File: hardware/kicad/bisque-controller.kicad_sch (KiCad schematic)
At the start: 52 parts, among them J1 USB-C, J2 5V_IN, J3 TC_K, J4 SSR, J5 DISPLAY, J6 NAV_SW, J7 AUX, Q1 AO3400A, Q2 AO3400A, SW1 RESET, SW2 BOOT, U1 ESP32-S3-WROOM-1-N16R8, U2 AMS1117-3.3, U3 MAX31855KASA+, U4 USBLC6-2SC6

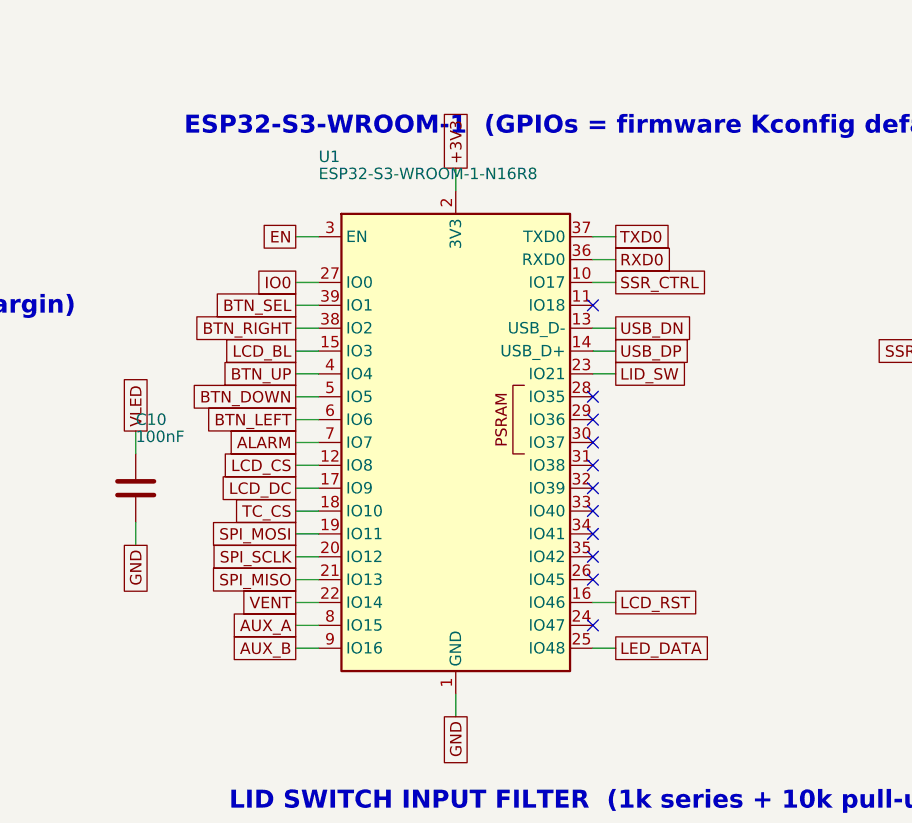
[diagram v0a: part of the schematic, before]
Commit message: feat(hw)!: re-map GPIOs for rev B
Buttons to 38-42 (contiguous module pads), lid to GPIO 4, SSR2 onto 21,
TC2/watchdog onto the pins quad PSRAM freed. check_pinmap.py now passes.
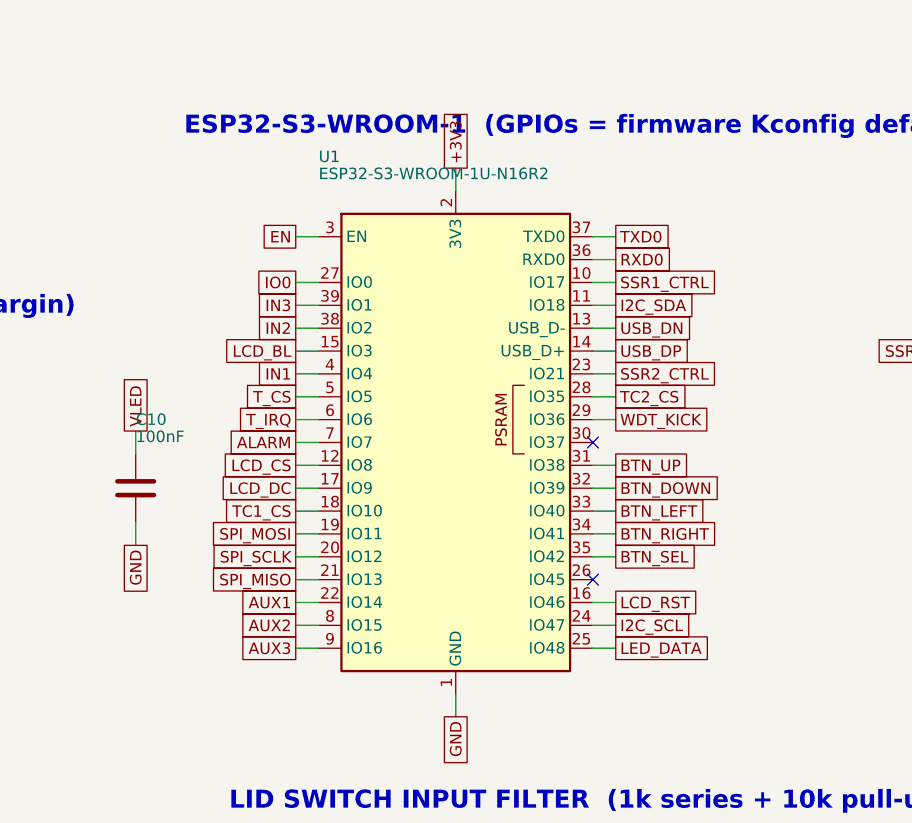
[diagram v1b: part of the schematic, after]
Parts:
- U1: value ESP32-S3-WROOM-1-N16R8 -> ESP32-S3-WROOM-1U-N16R2; footprint RF_Module:ESP32-S3-WROOM-1 -> RF_Module:ESP32-S3-WROOM-1U
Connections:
- net AUX_A: no longer U1.8 (IO15)
- net AUX_B: no longer U1.9 (IO16)
- net BTN_DOWN: now also U1.32 (IO39); no longer U1.5 (IO5)
- net BTN_LEFT: now also U1.33 (IO40); no longer U1.6 (IO6)
- net BTN_RIGHT: now also U1.34 (IO41); no longer U1.38 (IO2)
- net BTN_SEL: now also U1.35 (IO42); no longer U1.39 (IO1)
- net BTN_UP: now also U1.31 (IO38); no longer U1.4 (IO4)
- net LID_SW: no longer U1.23 (IO21)
- net SSR_CTRL: no longer U1.10 (IO17)
- net TC_CS: no longer U1.18 (IO10)
- net VENT: no longer U1.22 (IO14)
- net I2C_SDA: now reaches U1.11 (IO18)
- net I2C_SCL: now reaches U1.24 (IO47)
- net TC2_CS: now reaches U1.28 (IO35)
- net WDT_KICK: now reaches U1.29 (IO36)
- new net AUX1: U1.22 (IO14)
- new net AUX2: U1.8 (IO15)
- new net AUX3: U1.9 (IO16)
- new net IN1: U1.4 (IO4)
- new net IN2: U1.38 (IO2)
- new net IN3: U1.39 (IO1)
- new net SSR1_CTRL: U1.10 (IO17)
- new net SSR2_CTRL: U1.23 (IO21)
- new net TC1_CS: U1.18 (IO10)
- new net T_CS: U1.5 (IO5)
- new net T_IRQ: U1.6 (IO6)
- no-connect marks 15 -> 6
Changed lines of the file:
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@@
 			(effects (font (size 1.27 1.27)) (justify left))
 		)
-		(property "Value" "ESP32-S3-WROOM-1-N16R8" (at 154.94 135.25 0)
+		(property "Value" "ESP32-S3-WROOM-1U-N16R2" (at 154.94 135.25 0)
 			(effects (font (size 1.27 1.27)) (justify left))
 		)
-		(property "Footprint" "RF_Module:ESP32-S3-WROOM-1" (at 170.18 165.1 0)
+		(property "Footprint" "RF_Module:ESP32-S3-WROOM-1U" (at 170.18 165.1 0)
 			(effects (font (size 1.27 1.27)) hide)
 		)
@@
 		(stroke (width 0) (type default))
 	)
-	(global_label "BTN_UP" (shape passive) (at 152.4 157.48 180)
+	(global_label "IN1" (shape passive) (at 152.4 157.48 180)
 		(effects (font (size 1.27 1.27)) (justify right))
 		(property "Intersheetrefs" "${INTERSHEET_REFS}" (at 152.4 157.48 0)
@@
 		(stroke (width 0) (type default))
 	)
-	(global_label "BTN_DOWN" (shape passive) (at 152.4 160.02 180)
+	(global_label "T_CS" (shape passive) (at 152.4 160.02 180)
 		(effects (font (size 1.27 1.27)) (justify right))
 		(property "Intersheetrefs" "${INTERSHEET_REFS}" (at 152.4 160.02 0)
@@
 		(stroke (width 0) (type default))
 	)
-	(global_label "BTN_LEFT" (shape passive) (at 152.4 162.56 180)
+	(global_label "T_IRQ" (shape passive) (at 152.4 162.56 180)
 		(effects (font (size 1.27 1.27)) (justify right))
 		(property "Intersheetrefs" "${INTERSHEET_REFS}" (at 152.4 162.56 0)
@@
 		(stroke (width 0) (type default))
 	)
-	(global_label "AUX_A" (shape passive) (at 152.4 185.42 180)
+	(global_label "AUX2" (shape passive) (at 152.4 185.42 180)
 		(effects (font (size 1.27 1.27)) (justify right))
 		(property "Intersheetrefs" "${INTERSHEET_REFS}" (at 152.4 185.42 0)
@@
 		(stroke (width 0) (type default))
 	)
-	(global_label "AUX_B" (shape passive) (at 152.4 187.96 180)
+	(global_label "AUX3" (shape passive) (at 152.4 187.96 180)
 		(effects (font (size 1.27 1.27)) (justify right))
 		(property "Intersheetrefs" "${INTERSHEET_REFS}" (at 152.4 187.96 0)
@@
 		(stroke (width 0) (type default))
 	)
-	(global_label "SSR_CTRL" (shape passive) (at 187.96 147.32 0)
+	(global_label "SSR1_CTRL" (shape passive) (at 187.96 147.32 0)
 		(effects (font (size 1.27 1.27)) (justify left))
 		(property "Intersheetrefs" "${INTERSHEET_REFS}" (at 187.96 147.32 0)
@@
 		)
 	)
-	(no_connect (at 185.42 149.86))
+	(wire (pts (xy 185.42 149.86) (xy 187.96 149.86))
+		(stroke (width 0) (type default))
+	)
+	(global_label "I2C_SDA" (shape passive) (at 187.96 149.86 0)
+		(effects (font (size 1.27 1.27)) (justify left))
+		(property "Intersheetrefs" "${INTERSHEET_REFS}" (at 187.96 149.86 0)
+			(effects (font (size 1.27 1.27)) hide)
+		)
+	)
 	(wire (pts (xy 154.94 167.64) (xy 152.4 167.64))
 		(stroke (width 0) (type default))
@@
 		(stroke (width 0) (type default))
 	)
-	(global_label "TC_CS" (shape passive) (at 152.4 172.72 180)
+	(global_label "TC1_CS" (shape passive) (at 152.4 172.72 180)
 		(effects (font (size 1.27 1.27)) (justify right))
 		(property "Intersheetrefs" "${INTERSHEET_REFS}" (at 152.4 172.72 0)
@@
 		(stroke (width 0) (type default))
 	)
-	(global_label "VENT" (shape passive) (at 152.4 182.88 180)
+	(global_label "AUX1" (shape passive) (at 152.4 182.88 180)
 		(effects (font (size 1.27 1.27)) (justify right))
 		(property "Intersheetrefs" "${INTERSHEET_REFS}" (at 152.4 182.88 0)
@@
 		(stroke (width 0) (type default))
 	)
-	(global_label "LID_SW" (shape passive) (at 187.96 157.48 0)
+	(global_label "SSR2_CTRL" (shape passive) (at 187.96 157.48 0)
 		(effects (font (size 1.27 1.27)) (justify left))
 		(property "Intersheetrefs" "${INTERSHEET_REFS}" (at 187.96 157.48 0)
@@
 		)
 	)
-	(no_connect (at 185.42 185.42))
+	(wire (pts (xy 185.42 185.42) (xy 187.96 185.42))
+		(stroke (width 0) (type default))
+	)
+	(global_label "I2C_SCL" (shape passive) (at 187.96 185.42 0)
+		(effects (font (size 1.27 1.27)) (justify left))
+		(property "Intersheetrefs" "${INTERSHEET_REFS}" (at 187.96 185.42 0)
+			(effects (font (size 1.27 1.27)) hide)
+		)
+	)
 	(wire (pts (xy 185.42 187.96) (xy 187.96 187.96))
 		(stroke (width 0) (type default))
@@
 		)
 	)
-	(no_connect (at 185.42 160.02))
-	(no_connect (at 185.42 162.56))
+	(wire (pts (xy 185.42 160.02) (xy 187.96 160.02))
+		(stroke (width 0) (type default))
+	)
+	(global_label "TC2_CS" (shape passive) (at 187.96 160.02 0)
+		(effects (font (size 1.27 1.27)) (justify left))
+		(property "Intersheetrefs" "${INTERSHEET_REFS}" (at 187.96 160.02 0)
+			(effects (font (size 1.27 1.27)) hide)
+		)
+	)
+	(wire (pts (xy 185.42 162.56) (xy 187.96 162.56))
+		(stroke (width 0) (type default))
+	)
+	(global_label "WDT_KICK" (shape passive) (at 187.96 162.56 0)
+		(effects (font (size 1.27 1.27)) (justify left))
+		(property "Intersheetrefs" "${INTERSHEET_REFS}" (at 187.96 162.56 0)
+			(effects (font (size 1.27 1.27)) hide)
+		)
+	)
 	(no_connect (at 185.42 165.1))
-	(no_connect (at 185.42 167.64))
-	(no_connect (at 185.42 170.18))
-	(no_connect (at 185.42 172.72))
-	(no_connect (at 185.42 175.26))
-	(no_connect (at 185.42 177.8))
+	(wire (pts (xy 185.42 167.64) (xy 187.96 167.64))
+		(stroke (width 0) (type default))
+	)
+	(global_label "BTN_UP" (shape passive) (at 187.96 167.64 0)
+		(effects (font (size 1.27 1.27)) (justify left))
+		(property "Intersheetrefs" "${INTERSHEET_REFS}" (at 187.96 167.64 0)
+			(effects (font (size 1.27 1.27)) hide)
+		)
+	)
+	(wire (pts (xy 185.42 170.18) (xy 187.96 170.18))
+		(stroke (width 0) (type default))
+	)
+	(global_label "BTN_DOWN" (shape passive) (at 187.96 170.18 0)
+		(effects (font (size 1.27 1.27)) (justify left))
+		(property "Intersheetrefs" "${INTERSHEET_REFS}" (at 187.96 170.18 0)
+			(effects (font (size 1.27 1.27)) hide)
+		)
+	)
+	(wire (pts (xy 185.42 172.72) (xy 187.96 172.72))
+		(stroke (width 0) (type default))
+	)
+	(global_label "BTN_LEFT" (shape passive) (at 187.96 172.72 0)
+		(effects (font (size 1.27 1.27)) (justify left))
+		(property "Intersheetrefs" "${INTERSHEET_REFS}" (at 187.96 172.72 0)
+			(effects (font (size 1.27 1.27)) hide)
+		)
+	)
+	(wire (pts (xy 185.42 175.26) (xy 187.96 175.26))
+		(stroke (width 0) (type default))
+	)
+	(global_label "BTN_RIGHT" (shape passive) (at 187.96 175.26 0)
+		(effects (font (size 1.27 1.27)) (justify left))
+		(property "Intersheetrefs" "${INTERSHEET_REFS}" (at 187.96 175.26 0)
+			(effects (font (size 1.27 1.27)) hide)
+		)
+	)
+	(wire (pts (xy 185.42 177.8) (xy 187.96 177.8))
+		(stroke (width 0) (type default))
+	)
+	(global_label "BTN_SEL" (shape passive) (at 187.96 177.8 0)
+		(effects (font (size 1.27 1.27)) (justify left))
+		(property "Intersheetrefs" "${INTERSHEET_REFS}" (at 187.96 177.8 0)
+			(effects (font (size 1.27 1.27)) hide)
+		)
+	)
 	(wire (pts (xy 185.42 144.78) (xy 187.96 144.78))
 		(stroke (width 0) (type default))
@@
 		(stroke (width 0) (type default))
 	)
-	(global_label "BTN_RIGHT" (shape passive) (at 152.4 152.4 180)
+	(global_label "IN2" (shape passive) (at 152.4 152.4 180)
 		(effects (font (size 1.27 1.27)) (justify right))
 		(property "Intersheetrefs" "${INTERSHEET_REFS}" (at 152.4 152.4 0)
@@
 		(stroke (width 0) (type default))
 	)
-	(global_label "BTN_SEL" (shape passive) (at 152.4 149.86 180)
+	(global_label "IN3" (shape passive) (at 152.4 149.86 180)
 		(effects (font (size 1.27 1.27)) (justify right))
 		(property "Intersheetrefs" "${INTERSHEET_REFS}" (at 152.4 149.86 0)

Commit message: feat(hw): two MAX31856 thermocouple front-ends
Replaces the MAX31855 (U3/C8/C9) with two MAX31856 channels (U3 control,
U5 load), each with separate AVDD/DVDD decoupling, a 100R 1% series R in
each T+/T- leg, and the datasheet's differential (100nF) + common-mode
(10nF x2) input filter on the IC side of those resistors. DRDY and FAULT
left NC and polled from registers to save four GPIOs.

Per REV-B-NOTES.md (datasheet-verification override of the plan): there is
no BIAS bypass capacitor - BIAS ties directly to the filtered T- node
instead, matching the MAX31856's actual application circuit. TC1_N/TC2_N
run to their screw terminals raw, not to GND, so each channel keeps its own
floating differential pair; ungrounded-junction probes are now required
(documentation obligation, tracked for a later task).

Also fixes two now-dead net-name references in gen_pcb.py's ROUTE_ORDER
(TC_P, TC_CS) left over from the old MAX31855 wiring, and adds the TSSOP-14
footprint snapshot gen_pcb.py's KiCad-free fallback path requires.
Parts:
- removed C8: 100nF, Capacitor_SMD:C_0805_2012Metric, symbol Device:C
- removed C9: 10nF, Capacitor_SMD:C_0805_2012Metric, symbol Device:C
- added C13, C14, C15, C18, C19, C20: 100nF, Capacitor_SMD:C_0805_2012Metric, symbol Device:C
- added C16, C17, C21, C22: 10nF, Capacitor_SMD:C_0805_2012Metric, symbol Device:C
- added J8: TC2_K, TerminalBlock_Phoenix:TerminalBlock_Phoenix_MKDS-1,5-2-5.08_1x02_P5.08mm_Horizontal, symbol Connector:Screw_Terminal_01x02
- added R14, R15, R16, R17: 100R 1%, Resistor_SMD:R_0805_2012Metric, symbol Device:R
- added U5: MAX31856MUD+, Package_SO:TSSOP-14_4.4x5mm_P0.65mm, symbol Sensor_Temperature:MAX31856
- J3: value TC_K -> TC1_K
- U3: value MAX31855KASA+ -> MAX31856MUD+; footprint Package_SO:SOIC-8_3.9x4.9mm_P1.27mm -> Package_SO:TSSOP-14_4.4x5mm_P0.65mm; symbol Sensor_Temperature:MAX31855KASA -> Sensor_Temperature:MAX31856
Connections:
- net +3V3: now also U3.5 (AVDD), U3.8 (DVDD), C13.1, C14.1, C18.1, C19.1, U5.5 (AVDD), U5.8 (DVDD); no longer U3.4 (V_{CC})
- net GND: now also U3.14 (DGND), C13.2, C14.2, C16.2, C17.2, C18.2, C19.2, C21.2, C22.2, U5.1 (AGND), U5.14 (DGND); no longer J3.2 (Pin_2), U3.2 (T-)
- net SPI_MISO: now also U3.11 (SDO), U5.11 (SDO); no longer U3.7 (SO)
- net SPI_MOSI: now also U3.12 (SDI), U5.12 (SDI)
- net SPI_SCLK: now also U3.10 (SCK), U5.10 (SCK); no longer U3.5 (SCK)
- net TC1_CS: now also U3.9 (~{CS})
- net TC2_CS: now also U5.9 (~{CS})
- net TC_CS: no longer names the net of U3.6 (DNC)
- net TC_P renamed TC1_BIAS
- net TC1_BIAS: now also U3.2 (BIAS), C15.2, C17.1, R15.2; no longer J3.1 (Pin_1)
- new net TC1_N: J3.2 (Pin_2), R15.1
- new net TC1_P: J3.1 (Pin_1), R14.1
- new net TC1_P_F: C15.1, C16.1, R14.2, U3.4 (T+)
- new net TC2_BIAS: C20.2, C22.1, R17.2, U5.2 (BIAS), U5.3 (T-)
- new net TC2_N: J8.2 (Pin_2), R17.1
- new net TC2_P: J8.1 (Pin_1), R16.1
- new net TC2_P_F: C20.1, C21.1, R16.2, U5.4 (T+)
- no-connect marks 6 -> 11
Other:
- note added: "Bisque kiln controller - ESP32-S3-WROOM-1 SSR terminal J4: +5V / SSR- loop, switched low-side by Q1 (boot-safe: R7 pulldown) TC1 terminal J3 / TC2 terminal J8: pin1 = K+, pin2 = K- - both float, biased near AGND only through each MAX31856's internal BIAS network. Ungrounded-junction probes required: two grounded-junction probes in one kiln would loop through it. Nav switch J6 is panel-mounted; in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"
- note added: "THERMOCOUPLE 1 (control) MAX31856 (T- floats to J3, biased via BIAS)"
- note added: "THERMOCOUPLE 2 (load) MAX31856 (T- floats to J8, biased via BIAS)"
- note removed: "Bisque kiln controller - ESP32-S3-WROOM-1 SSR terminal J4: +5V / SSR- loop, switched low-side by Q1 (boot-safe: R7 pulldown) TC terminal J3: pin1 = K+ (yellow), pin2 = K- (red, grounded at U3) Nav switch J6 is panel-mounted; inputs use ESP32 internal pull-ups Aux J7 pin6 = optional lid switch (dry contact to J7 pin2/GND, closed = lid shut) Display J5 pinout: 3V3 GND CS RST DC MOSI SCK BL (ST7796S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"
- note removed: "THERMOCOUPLE MAX31855 (T- grounded per datasheet)"
- moved on the sheet: J3

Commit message: fix(hw): put MAX31856 BIAS on the raw terminal node, not filtered T-
Review caught that BIAS (pin 2) was merged onto the IC-side filtered T-
node (TC1_BIAS/TC2_BIAS), matching the datasheet's simple Typical
Application Circuit rather than Figure 8, the filtered topology this
board actually uses. REV-B-NOTES.md SS5a is explicit that in Figure 8
"BIAS connects to the thermocouple side of the resistor" - the raw
terminal-side node, upstream of the 100R series R, not the filtered pin.

BIAS now joins TC1_N/TC2_N (raw, terminal-side). T- keeps its own IC-side
filtered node, renamed TC1_N_F/TC2_N_F (symmetric with TC1_P_F/TC2_P_F).
Filter capacitor placement is unchanged. No TC1_BIAS/TC2_BIAS net remains.
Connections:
- net TC1_N: now also U3.2 (BIAS)
- net TC2_N: now also U5.2 (BIAS)
- net TC1_BIAS renamed TC1_N_F
- net TC1_N_F: no longer U3.2 (BIAS)
- net TC2_BIAS renamed TC2_N_F
- net TC2_N_F: no longer U5.2 (BIAS)
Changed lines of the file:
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@@
 		(stroke (width 0) (type default))
 	)
-	(global_label "TC1_BIAS" (shape passive) (at 234.95 97.79 180)
+	(global_label "TC1_N" (shape passive) (at 234.95 97.79 180)
 		(effects (font (size 1.27 1.27)) (justify right))
 		(property "Intersheetrefs" "${INTERSHEET_REFS}" (at 234.95 97.79 0)
@@
 		(stroke (width 0) (type default))
 	)
-	(global_label "TC1_BIAS" (shape passive) (at 234.95 95.25 180)
+	(global_label "TC1_N_F" (shape passive) (at 234.95 95.25 180)
 		(effects (font (size 1.27 1.27)) (justify right))
 		(property "Intersheetrefs" "${INTERSHEET_REFS}" (at 234.95 95.25 0)
@@
 		(stroke (width 0) (type default))
 	)
-	(global_label "TC1_BIAS" (shape passive) (at 322.58 101.6 270)
+	(global_label "TC1_N_F" (shape passive) (at 322.58 101.6 270)
 		(effects (font (size 1.27 1.27)) (justify right))
 		(property "Intersheetrefs" "${INTERSHEET_REFS}" (at 322.58 101.6 0)
@@
 		(stroke (width 0) (type default))
 	)
-	(global_label "TC1_BIAS" (shape passive) (at 340.36 101.6 270)
+	(global_label "TC1_N_F" (shape passive) (at 340.36 101.6 270)
 		(effects (font (size 1.27 1.27)) (justify right))
 		(property "Intersheetrefs" "${INTERSHEET_REFS}" (at 340.36 101.6 0)
@@
 		(stroke (width 0) (type default))
 	)
-	(global_label "TC1_BIAS" (shape passive) (at 375.92 88.9 90)
+	(global_label "TC1_N_F" (shape passive) (at 375.92 88.9 90)
 		(effects (font (size 1.27 1.27)) (justify left))
 		(property "Intersheetrefs" "${INTERSHEET_REFS}" (at 375.92 88.9 0)
@@
 		(stroke (width 0) (type default))
 	)
-	(global_label "TC2_BIAS" (shape passive) (at 234.95 137.16 180)
+	(global_label "TC2_N" (shape passive) (at 234.95 137.16 180)
 		(effects (font (size 1.27 1.27)) (justify right))
 		(property "Intersheetrefs" "${INTERSHEET_REFS}" (at 234.95 137.16 0)
@@
 		(stroke (width 0) (type default))
 	)
-	(global_label "TC2_BIAS" (shape passive) (at 234.95 134.62 180)
+	(global_label "TC2_N_F" (shape passive) (at 234.95 134.62 180)
 		(effects (font (size 1.27 1.27)) (justify right))
 		(property "Intersheetrefs" "${INTERSHEET_REFS}" (at 234.95 134.62 0)
@@
 		(stroke (width 0) (type default))
 	)
-	(global_label "TC2_BIAS" (shape passive) (at 322.58 140.97 270)
+	(global_label "TC2_N_F" (shape passive) (at 322.58 140.97 270)
 		(effects (font (size 1.27 1.27)) (justify right))
 		(property "Intersheetrefs" "${INTERSHEET_REFS}" (at 322.58 140.97 0)
@@
 		(stroke (width 0) (type default))
 	)
-	(global_label "TC2_BIAS" (shape passive) (at 340.36 140.97 270)
+	(global_label "TC2_N_F" (shape passive) (at 340.36 140.97 270)
 		(effects (font (size 1.27 1.27)) (justify right))
 		(property "Intersheetrefs" "${INTERSHEET_REFS}" (at 340.36 140.97 0)
@@
 		(stroke (width 0) (type default))
 	)
-	(global_label "TC2_BIAS" (shape passive) (at 375.92 128.27 90)
+	(global_label "TC2_N_F" (shape passive) (at 375.92 128.27 90)
 		(effects (font (size 1.27 1.27)) (justify left))
 		(property "Intersheetrefs" "${INTERSHEET_REFS}" (at 375.92 128.27 0)
